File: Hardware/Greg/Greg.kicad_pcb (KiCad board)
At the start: 2 copper layers, 30 x 24 mm, 40 parts, among them IC1 TPS61089RNRR, IC2 AP2205-W5-7, J1 1053131104, J3 Conn_01x08_Pin

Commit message: updated resistor values for 1.1v ref
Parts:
- R13: value 49 -> 44.2
- R9: value 75k -> 86.6k
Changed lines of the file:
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@@
 			)
 		)
+		(sheetname "Root")
+		(sheetfile "Greg.kicad_sch")
 		(attr smd)
 		(fp_poly
@@
 			)
 		)
-		(property "Value" "49"
+		(property "Value" "44.2"
 			(at 0 1.17 -90)
 			(layer "F.Fab")
@@
 			)
 		)
-		(property "Value" "75k"
+		(property "Value" "86.6k"
 			(at 0 1.17 90)
 			(layer "F.Fab")
@@
 	)
 	(zone
-		(net 2)
-		(net_name "Net-(JP4-B)")
+		(net 3)
+		(net_name "Net-(JP1-C)")
 		(layer "F.Cu")
 		(name "$teardrop_padvia$")
 		(hatch full 0.1)
-		(priority 30001)
+		(priority 30021)
 		(attr
 			(teardrop
@@
 		(polygon
 			(pts
-				(xy 142.38 90.398681) (xy 142.58 90.398681) (xy 143.729259 89.832123) (xy 143.27 88.869) (xy 142.420994 88.660542)
+				(xy 144.007885 92.450694) (xy 144.149306 92.592115) (xy 144.560399 92.35) (xy 144.470708 92.029293)
+				(xy 144.200001 91.935765)
 			)
 		)
 	)
 	(zone
-		(net 3)
-		(net_name "Net-(JP1-C)")
+		(net 23)
+		(net_name "Net-(JP2-C)")
 		(layer "F.Cu")
 		(name "$teardrop_padvia$")
 		(hatch full 0.1)
-		(priority 30021)
+		(priority 30000)
 		(attr
 			(teardrop
@@
 		(polygon
 			(pts
-				(xy 144.007885 92.450694) (xy 144.149306 92.592115) (xy 144.560399 92.35) (xy 144.470708 92.029293)
-				(xy 144.200001 91.935765)
+				(xy 139.307882 89.925441) (xy 139.449303 90.066862) (xy 140.782069 89.953667) (xy 140.770707 88.869293)
+				(xy 139.93824 88.449568)
 			)
 		)
@@
 	)
 	(zone
-		(net 2)
-		(net_name "Net-(JP4-B)")
-		(layer "F.Cu")
-		(name "$teardrop_padvia$")
-		(hatch full 0.1)
-		(priority 30040)
-		(attr
-			(teardrop
-				(type padvia)
-			)
-		)
-		(connect_pads yes
-			(clearance 0)
-		)
-		(min_thickness 0.0254)
-		(filled_areas_thickness no)
-		(fill yes
-			(thermal_gap 0.5)
-			(thermal_bridge_width 0.5)
-			(island_removal_mode 1)
-			(island_area_min 10)
-		)
-		(polygon
-			(pts
-				(xy 144.15 91.17) (xy 144.149999 90.970001) (xy 143.796662 90.810277) (xy 143.559001 91.070001)
-				(xy 143.796662 91.329725)
-			)
-		)
-	)
-	(zone
-		(net 18)
-		(net_name "Net-(JP1-B)")
-		(layer "F.Cu")
-		(name "$teardrop_padvia$")
-		(hatch full 0.1)
-		(priority 30050)
-		(attr
-			(teardrop
-				(type padvia)
-			)
-		)
-		(connect_pads yes
-			(clearance 0)
-		)
-		(min_thickness 0.0254)
-		(filled_areas_thickness no)
-		(fill yes
-			(thermal_gap 0.5)
-			(thermal_bridge_width 0.5)
-			(island_removal_mode 1)
-			(island_area_min 10)
-		)
-		(polygon
-			(pts
-				(xy 135.692313 94.040707) (xy 135.848679 93.916009) (xy 135.9 93.614999) (xy 135.579377 93.479218)
-				(xy 135.393855 93.749771)
-			)
-		)
-	)
-	(zone
 		(net 9)
 		(net_name "/FB_5V")
@@
 	)
 	(zone
-		(net 4)
-		(net_name "Net-(JP3-A)")
+		(net 6)
+		(net_name "Net-(IC2-ADJ{slash}NC)")
 		(layer "F.Cu")
 		(name "$teardrop_padvia$")
 		(hatch full 0.1)
-		(priority 30028)
+		(priority 30042)
 		(attr
 			(teardrop
@@
 		(polygon
 			(pts
-				(xy 142.978371 92.320208) (xy 143.119792 92.461629) (xy 143.633173 92.359999) (xy 143.560707 92.089292)
-				(xy 143.24 91.964934)
+				(xy 132.940429 96.626349) (xy 132.742892 96.595061) (xy 132.536476 96.84) (xy 132.829844 97.140987)
+				(xy 133.136626 96.84)
 			)
 		)
 	)
 	(zone
-		(net 6)
-		(net_name "Net-(IC2-ADJ{slash}NC)")
+		(net 22)
+		(net_name "+5V")
 		(layer "F.Cu")
 		(name "$teardrop_padvia$")
 		(hatch full 0.1)
-		(priority 30042)
+		(priority 30002)
 		(attr
 			(teardrop
@@
 		(polygon
 			(pts
-				(xy 132.940429 96.626349) (xy 132.742892 96.595061) (xy 132.536476 96.84) (xy 132.829844 97.140987)
-				(xy 133.136626 96.84)
+				(xy 136.578228 88.815238) (xy 136.612956 89.012198) (xy 137.424434 89.742295) (xy 138.270984 88.869827)
+				(xy 137.42 88.041829)
 			)
 		)
@@
 	)
 	(zone
+		(net 4)
+		(net_name "Net-(JP3-A)")
+		(layer "F.Cu")
+		(name "$teardrop_padvia$")
+		(hatch full 0.1)
+		(priority 30003)
+		(attr
+			(teardrop
+				(type padvia)
+			)
+		)
+		(connect_pads yes
+			(clearance 0)
+		)
+		(min_thickness 0.0254)
+		(filled_areas_thickness no)
+		(fill yes
+			(thermal_gap 0.5)
+			(thermal_bridge_width 0.5)
+			(island_removal_mode 1)
+			(island_area_min 10)
+		)
+		(polygon
+			(pts
+				(xy 142.978371 92.320208) (xy 143.119792 92.461629) (xy 143.633173 92.359999) (xy 143.560707 92.089292)
+				(xy 143.24 91.964934)
+			)
+		)
+	)
+	(zone
 		(net 12)
 		(net_name "/SW_5V")
@@
 	)
 	(zone
+		(net 19)
+		(net_name "Net-(JP2-B)")
+		(layer "F.Cu")
+		(name "$teardrop_padvia$")
+		(hatch full 0.1)
+		(priority 30007)
+		(attr
+			(teardrop
+				(type padvia)
+			)
+		)
+		(connect_pads yes
+			(clearance 0)
+		)
+		(min_thickness 0.0254)
+		(filled_areas_thickness no)
+		(fill yes
+			(thermal_gap 0.5)
+			(thermal_bridge_width 0.5)
+			(island_removal_mode 1)
+			(island_area_min 10)
+		)
+		(polygon
+			(pts
+				(xy 135.85087 92.024697) (xy 135.694504 91.899999) (xy 135.394783 92.190044) (xy 135.579377 92.460782)
+				(xy 135.9 92.325001)
+			)
+		)
+	)
+	(zone
 		(net 5)
 		(net_name "/LDO5.5V_IN")
@@
 	)
 	(zone
-		(net 22)
-		(net_name "+5V")
+		(net 2)
+		(net_name "Net-(JP4-B)")
 		(layer "F.Cu")
 		(name "$teardrop_padvia$")
 		(hatch full 0.1)
-		(priority 30002)
+		(priority 30001)
 		(attr
 			(teardrop
@@
 		(polygon
 			(pts
-				(xy 136.578228 88.815238) (xy 136.612956 89.012198) (xy 137.424434 89.742295) (xy 138.270984 88.869827)
-				(xy 137.42 88.041829)
+				(xy 142.38 90.398681) (xy 142.58 90.398681) (xy 143.729259 89.832123) (xy 143.27 88.869) (xy 142.420994 88.660542)
 			)
 		)
@@
 	)
 	(zone
-		(net 19)
-		(net_name "Net-(JP2-B)")
-		(layer "F.Cu")
-		(name "$teardrop_padvia$")
-		(hatch full 0.1)
-		(priority 30051)
-		(attr
-			(teardrop
-				(type padvia)
-			)
-		)
-		(connect_pads yes
-			(clearance 0)
-		)
-		(min_thickness 0.0254)
-		(filled_areas_thickness no)
-		(fill yes
-			(thermal_gap 0.5)
-			(thermal_bridge_width 0.5)
-			(island_removal_mode 1)
-			(island_area_min 10)
-		)
-		(polygon
-			(pts
-				(xy 135.85087 92.024697) (xy 135.694504 91.899999) (xy 135.394783 92.190044) (xy 135.579377 92.460782)
-				(xy 135.9 92.325001)
-			)
-		)
-	)
-	(zone
 		(net 14)
 		(net_name "Net-(IC1-EN)")
@@
 		(name "$teardrop_padvia$")
 		(hatch full 0.1)
-		(priority 30036)
-		(attr
-			(teardrop
-				(type padvia)
-			)
-		)
-		(connect_pads yes
-			(clearance 0)
-		)
-		(min_thickness 0.0254)
-		(filled_areas_thickness no)
-		(fill yes
-			(thermal_gap 0.5)
-			(thermal_bridge_width 0.5)
-			(island_removal_mode 1)
-			(island_area_min 10)
-		)
-		(polygon
-			(pts
-				(xy 142.97 90.970001) (xy 142.97 91.170001) (xy 143.323338 91.329725) (xy 143.561 91.070001) (xy 143.323338 90.810277)
-			)
-		)
-	)
-	(zone
-		(net 2)
-		(net_name "Net-(JP4-B)")
-		(layer "F.Cu")
-		(name "$teardrop_padvia$")
-		(hatch full 0.1)
 		(priority 30012)
 		(attr
@@
 	)
 	(zone
+		(net 18)
+		(net_name "Net-(JP1-B)")
+		(layer "F.Cu")
+		(name "$teardrop_padvia$")
+		(hatch full 0.1)
+		(priority 30006)
+		(attr
+			(teardrop
+				(type padvia)
+			)
+		)
+		(connect_pads yes
+			(clearance 0)
+		)
+		(min_thickness 0.0254)
+		(filled_areas_thickness no)
+		(fill yes
+			(thermal_gap 0.5)
+			(thermal_bridge_width 0.5)
+			(island_removal_mode 1)
+			(island_area_min 10)
+		)
+		(polygon
+			(pts
+				(xy 135.692313 94.040707) (xy 135.848679 93.916009) (xy 135.9 93.614999) (xy 135.579377 93.479218)
+				(xy 135.393855 93.749771)
+			)
+		)
+	)
+	(zone
 		(net 8)
 		(net_name "+3V3")
@@
 	)
 	(zone
-		(net 23)
-		(net_name "Net-(JP2-C)")
+		(net 2)
+		(net_name "Net-(JP4-B)")
 		(layer "F.Cu")
 		(name "$teardrop_padvia$")
 		(hatch full 0.1)
-		(priority 30000)
+		(priority 30005)
 		(attr
 			(teardrop
@@
 		(polygon
 			(pts
-				(xy 139.307882 89.925441) (xy 139.449303 90.066862) (xy 140.782069 89.953667) (xy 140.770707 88.869293)
-				(xy 139.93824 88.449568)
+				(xy 144.15 91.17) (xy 144.149999 90.970001) (xy 143.796662 90.810277) (xy 143.559001 91.070001)
+				(xy 143.796662 91.329725)
 			)
 		)
@@
 			)
 		)
+	)
+	(zone
+		(net 2)
+		(net_name "Net-(JP4-B)")
+		(layer "F.Cu")
+		(name "$teardrop_padvia$")
+		(hatch full 0.1)
+		(priority 30004)
+		(attr
+			(teardrop
+				(type padvia)
+			)
+		)
+		(connect_pads yes
+			(clearance 0)
+		)
+		(min_thickness 0.0254)
+		(filled_areas_thickness no)
+		(fill yes
+			(thermal_gap 0.5)
+			(thermal_bridge_width 0.5)
+			(island_removal_mode 1)
+			(island_area_min 10)
+		)
+		(polygon
+			(pts
+				(xy 142.97 90.970001) (xy 142.97 91.170001) (xy 143.323338 91.329725) (xy 143.561 91.070001) (xy 143.323338 90.810277)
+			)
+		)

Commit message: changed a cap
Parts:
- C11: footprint Capacitor_SMD:C_0402_1005Metric -> Capacitor_SMD:C_0603_1608Metric
- R7: value 152k -> 150k
- moved C4 1.45 mm to (136.1, 98.1)
- moved C8 0.98 mm to (131.0, 97.9)
- moved IC2 0.51 mm to (133.6, 98.1)
- moved C12 0.39 mm to (137.1, 98.1)
- moved C11 0.26 mm to (138.2, 98.1)

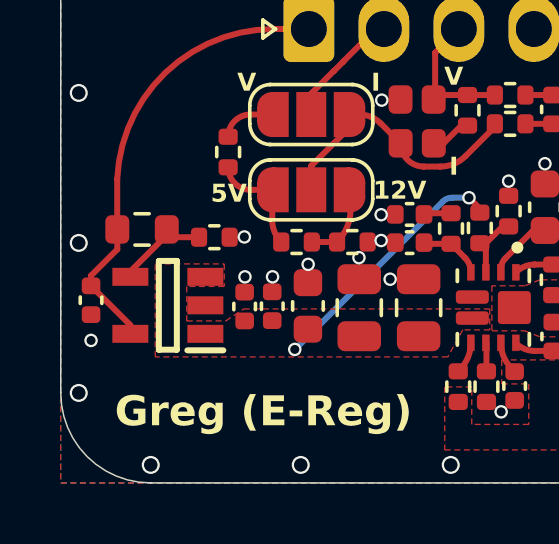
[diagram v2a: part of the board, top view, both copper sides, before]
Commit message: changed ldo resistor to match stark
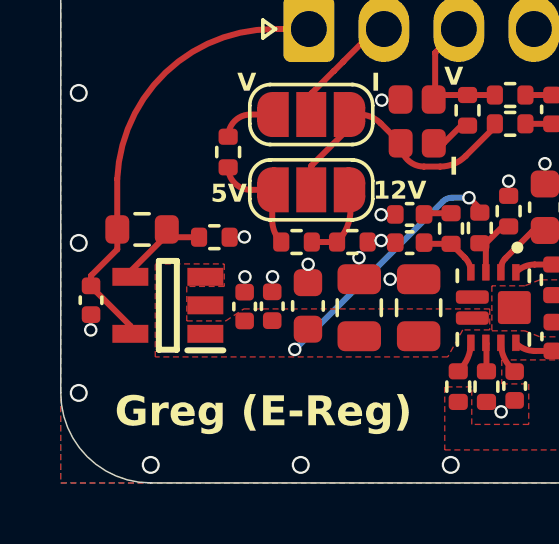
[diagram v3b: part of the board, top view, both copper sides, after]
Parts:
- R6: value 50k -> 49.9k
- R7: value 150k -> 152k

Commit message: changed non standard resistor on ldo
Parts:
- R7: value 152k -> 150k
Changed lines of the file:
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@@
 			)
 		)
-		(property "Value" "152k"
+		(property "Value" "150k"
 			(at 0 1.43 180)
 			(layer "F.Fab")
@@
 	)
 	(zone
-		(net 2)
-		(net_name "Net-(JP4-B)")
+		(net 6)
+		(net_name "Net-(IC2-ADJ{slash}NC)")
 		(layer "F.Cu")
 		(name "$teardrop_padvia$")
 		(hatch full 0.1)
-		(priority 30001)
+		(priority 30003)
 		(attr
 			(teardrop
@@
 		(polygon
 			(pts
-				(xy 142.38 90.398681) (xy 142.58 90.398681) (xy 143.729259 89.832123) (xy 143.27 88.869) (xy 142.420994 88.660542)
+				(xy 132.906379 96.2222) (xy 133.0478 96.363621) (xy 133.67864 96.025) (xy 133.535707 95.549293)
+				(xy 133.135 95.416727)
 			)
 		)
@@
 	)
 	(zone
+		(net 22)
+		(net_name "+5V")
+		(layer "F.Cu")
+		(name "$teardrop_padvia$")
+		(hatch full 0.1)
+		(priority 30006)
+		(attr
+			(teardrop
+				(type padvia)
+			)
+		)
+		(connect_pads yes
+			(clearance 0)
+		)
+		(min_thickness 0.0254)
+		(filled_areas_thickness no)
+		(fill yes
+			(thermal_gap 0.5)
+			(thermal_bridge_width 0.5)
+			(island_removal_mode 1)
+			(island_area_min 10)
+		)
+		(polygon
+			(pts
+				(xy 131.665797 96.292781) (xy 131.807219 96.434203) (xy 132.214466 95.974408) (xy 131.885707 95.549293)
+				(xy 131.500224 95.901537)
+			)
+		)
+	)
+	(zone
 		(net 11)
 		(net_name "Net-(IC1-VCC)")
@@
 	)
 	(zone
+		(net 6)
+		(net_name "Net-(IC2-ADJ{slash}NC)")
+		(layer "F.Cu")
+		(name "$teardrop_padvia$")
+		(hatch full 0.1)
+		(priority 30005)
+		(attr
+			(teardrop
+				(type padvia)
+			)
+		)
+		(connect_pads yes
+			(clearance 0)
+		)
+		(min_thickness 0.0254)
+		(filled_areas_thickness no)
+		(fill yes
+			(thermal_gap 0.5)
+			(thermal_bridge_width 0.5)
+			(island_removal_mode 1)
+			(island_area_min 10)
+		)
+		(polygon
+			(pts
+				(xy 134.335 95.91) (xy 134.335 95.71) (xy 133.931729 95.258555) (xy 133.534 95.55) (xy 133.735 96.025)
+			)
+		)
+	)
+	(zone
 		(net 17)
 		(net_name "Net-(JP1-A)")
@@
 	)
 	(zone
-		(net 6)
-		(net_name "Net-(IC2-ADJ{slash}NC)")
+		(net 22)
+		(net_name "+5V")
 		(layer "F.Cu")
 		(name "$teardrop_padvia$")
 		(hatch full 0.1)
-		(priority 30013)
+		(priority 30002)
 		(attr
 			(teardrop
@@
 		(polygon
 			(pts
-				(xy 134.335 95.91) (xy 134.335 95.71) (xy 133.931729 95.258555) (xy 133.534 95.55) (xy 133.735 96.025)
+				(xy 136.87496 88.772846) (xy 136.891961 88.972121) (xy 137.420296 89.721491) (xy 138.270996 88.869915)
+				(xy 137.42 88.021488)
 			)
 		)
@@
 	)
 	(zone
-		(net 23)
-		(net_name "Net-(JP2-C)")
-		(layer "F.Cu")
-		(name "$teardrop_padvia$")
-		(hatch full 0.1)
-		(priority 30000)
-		(attr
-			(teardrop
-				(type padvia)
-			)
-		)
-		(connect_pads yes
-			(clearance 0)
-		)
-		(min_thickness 0.0254)
-		(filled_areas_thickness no)
-		(fill yes
-			(thermal_gap 0.5)
-			(thermal_bridge_width 0.5)
-			(island_removal_mode 1)
-			(island_area_min 10)
-		)
-		(polygon
-			(pts
-				(xy 139.307882 89.925441) (xy 139.449303 90.066862) (xy 140.782069 89.953667) (xy 140.770707 88.869293)
-				(xy 139.93824 88.449568)
-			)
-		)
-	)
-	(zone
 		(net 15)
 		(net_name "Net-(IC1-ILIM)")
@@
 	)
 	(zone
-		(net 22)
-		(net_name "+5V")
-		(layer "F.Cu")
-		(name "$teardrop_padvia$")
-		(hatch full 0.1)
-		(priority 30015)
-		(attr
-			(teardrop
-				(type padvia)
-			)
-		)
-		(connect_pads yes
-			(clearance 0)
-		)
-		(min_thickness 0.0254)
-		(filled_areas_thickness no)
-		(fill yes
-			(thermal_gap 0.5)
-			(thermal_bridge_width 0.5)
-			(island_removal_mode 1)
-			(island_area_min 10)
-		)
-		(polygon
-			(pts
-				(xy 131.665797 96.292781) (xy 131.807219 96.434203) (xy 132.214466 95.974408) (xy 131.885707 95.549293)
-				(xy 131.500224 95.901537)
-			)
-		)
-	)
-	(zone
 		(net 16)
 		(net_name "/AIN0N")
@@
 	)
 	(zone
+		(net 2)
+		(net_name "Net-(JP4-B)")
+		(layer "F.Cu")
+		(name "$teardrop_padvia$")
+		(hatch full 0.1)
+		(priority 30001)
+		(attr
+			(teardrop
+				(type padvia)
+			)
+		)
+		(connect_pads yes
+			(clearance 0)
+		)
+		(min_thickness 0.0254)
+		(filled_areas_thickness no)
+		(fill yes
+			(thermal_gap 0.5)
+			(thermal_bridge_width 0.5)
+			(island_removal_mode 1)
+			(island_area_min 10)
+		)
+		(polygon
+			(pts
+				(xy 142.38 90.398681) (xy 142.58 90.398681) (xy 143.729259 89.832123) (xy 143.27 88.869) (xy 142.420994 88.660542)
+			)
+		)
+	)
+	(zone
 		(net 20)
 		(net_name "Net-(C3-Pad1)")
@@
 	)
 	(zone
-		(net 22)
-		(net_name "+5V")
-		(layer "F.Cu")
-		(name "$teardrop_padvia$")
-		(hatch full 0.1)
-		(priority 30004)
-		(attr
-			(teardrop
-				(type padvia)
-			)
-		)
-		(connect_pads yes
-			(clearance 0)
-		)
-		(min_thickness 0.0254)
-		(filled_areas_thickness no)
-		(fill yes
-			(thermal_gap 0.5)
-			(thermal_bridge_width 0.5)
-			(island_removal_mode 1)
-			(island_area_min 10)
-		)
-		(polygon
-			(pts
-				(xy 136.87496 88.772846) (xy 136.891961 88.972121) (xy 137.420296 89.721491) (xy 138.270996 88.869915)
-				(xy 137.42 88.021488)
-			)
-		)
-	)
-	(zone
 		(net 3)
 		(net_name "Net-(JP1-C)")
@@
 	)
 	(zone
-		(net 22)
-		(net_name "+5V")
-		(layer "F.Cu")
-		(name "$teardrop_padvia$")
-		(hatch full 0.1)
-		(priority 30011)
-		(attr
-			(teardrop
-				(type padvia)
-			)
-		)
-		(connect_pads yes
-			(clearance 0)
-		)
-		(min_thickness 0.0254)
-		(filled_areas_thickness no)
-		(fill yes
-			(thermal_gap 0.5)
-			(thermal_bridge_width 0.5)
-			(island_removal_mode 1)
-			(island_area_min 10)
-		)
-		(polygon
-			(pts
-				(xy 131.982439 94.675) (xy 131.782439 94.675) (xy 131.500224 95.198463) (xy 131.885 95.551) (xy 132.269776 95.198463)
-			)
-		)
-	)
-	(zone
 		(net 0)
 		(net_name "")
@@
 	)
 	(zone
-		(net 6)
-		(net_name "Net-(IC2-ADJ{slash}NC)")
+		(net 13)
+		(net_name "Net-(IC1-COMP)")
 		(layer "F.Cu")
 		(name "$teardrop_padvia$")
 		(hatch full 0.1)
-		(priority 30008)
+		(priority 30054)
 		(attr
 			(teardrop
@@
 		(polygon
 			(pts
-				(xy 132.906379 96.2222) (xy 133.0478 96.363621) (xy 133.67864 96.025) (xy 133.535707 95.549293)
-				(xy 133.135 95.416727)
+				(xy 143.636391 96.539903) (xy 143.470096 96.651013) (xy 143.545 96.99761) (xy 143.670555 96.980831)
+				(xy 143.717253 96.705)
 			)
 		)
 	)
 	(zone
-		(net 13)
-		(net_name "Net-(IC1-COMP)")
+		(net 6)
+		(net_name "Net-(IC2-ADJ{slash}NC)")
 		(layer "F.Cu")
 		(name "$teardrop_padvia$")
 		(hatch full 0.1)
-		(priority 30054)
+		(priority 30042)
 		(attr
 			(teardrop
@@
 		(polygon
 			(pts
-				(xy 143.636391 96.539903) (xy 143.470096 96.651013) (xy 143.545 96.99761) (xy 143.670555 96.980831)
-				(xy 143.717253 96.705)
+				(xy 134.070002 95.71) (xy 134.070002 95.91) (xy 134.372554 96.08) (xy 134.611002 95.81) (xy 134.372554 95.54)
 			)
 		)
 	)
 	(zone
-		(net 6)
-		(net_name "Net-(IC2-ADJ{slash}NC)")
+		(net 22)
+		(net_name "+5V")
 		(layer "F.Cu")
 		(name "$teardrop_padvia$")
 		(hatch full 0.1)
-		(priority 30042)
+		(priority 30004)
 		(attr
 			(teardrop
@@
 		(polygon
 			(pts
-				(xy 134.070002 95.71) (xy 134.070002 95.91) (xy 134.372554 96.08) (xy 134.611002 95.81) (xy 134.372554 95.54)
+				(xy 131.982439 94.675) (xy 131.782439 94.675) (xy 131.500224 95.198463) (xy 131.885 95.551) (xy 132.269776 95.198463)
 			)
 		)
@@
 			)
 		)
+	)
+	(zone
+		(net 23)
+		(net_name "Net-(JP2-C)")
+		(layer "F.Cu")
+		(name "$teardrop_padvia$")
+		(hatch full 0.1)
+		(priority 30000)
+		(attr
+			(teardrop
+				(type padvia)
+			)
+		)
+		(connect_pads yes
+			(clearance 0)
+		)
+		(min_thickness 0.0254)
+		(filled_areas_thickness no)
+		(fill yes
+			(thermal_gap 0.5)
+			(thermal_bridge_width 0.5)
+			(island_removal_mode 1)
+			(island_area_min 10)
+		)
+		(polygon
+			(pts
+				(xy 139.307882 89.925441) (xy 139.449303 90.066862) (xy 140.782069 89.953667) (xy 140.770707 88.869293)
+				(xy 139.93824 88.449568)
+			)
+		)

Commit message: Ordering files
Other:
- board text added: "JLCJLCJLCJLC"
